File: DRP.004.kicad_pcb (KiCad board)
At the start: 4 copper layers, 55 x 27 mm, 79 parts, among them J1 Batt_conn_3p, J2 USB_C_Receptacle_PowerOnly_6P, J3 Conn_01x03_Pin, J4 Conn_01x05_Pin, J5 Conn_01x03_Pin, J6 Conn_01x03_Pin, Q1 DTC143Z, Q2 AO3400, Q3 DTC143Z, Q4 DMG1012T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

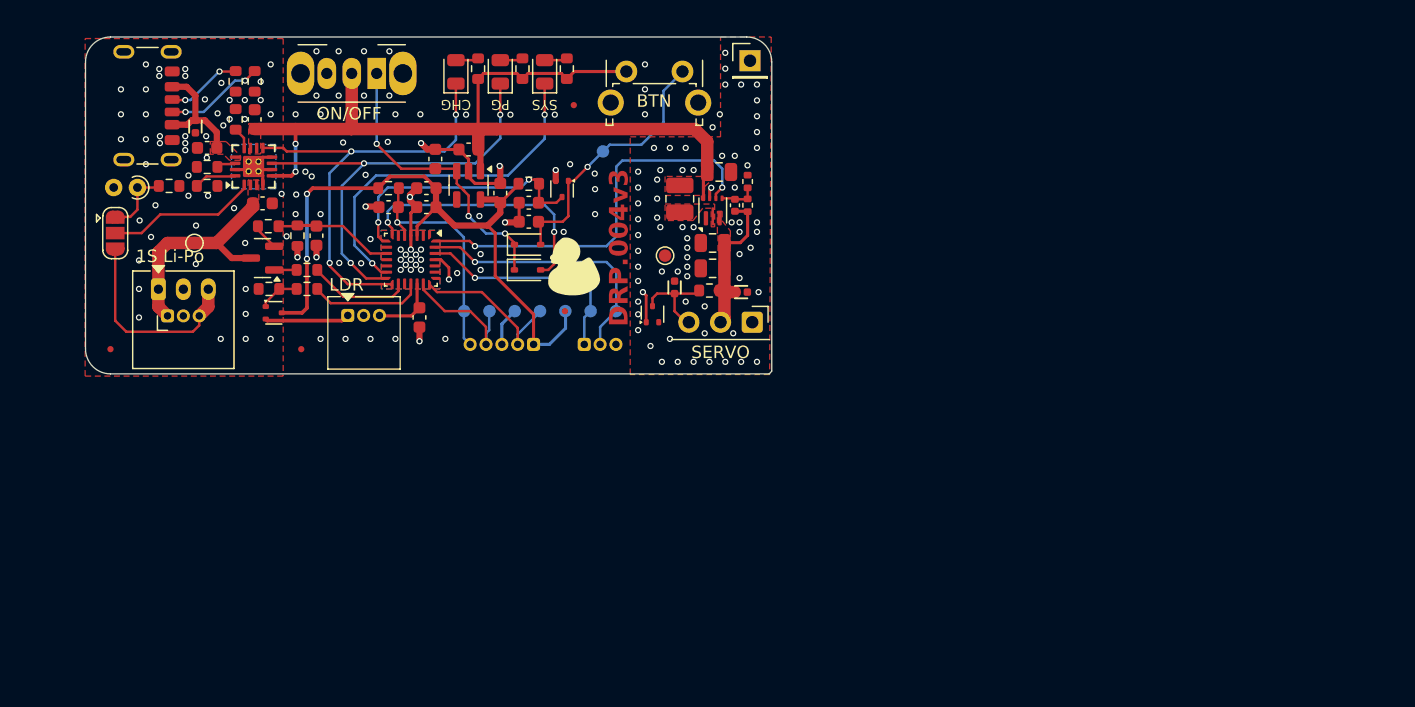
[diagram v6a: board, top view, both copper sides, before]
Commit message: Added stencil outline
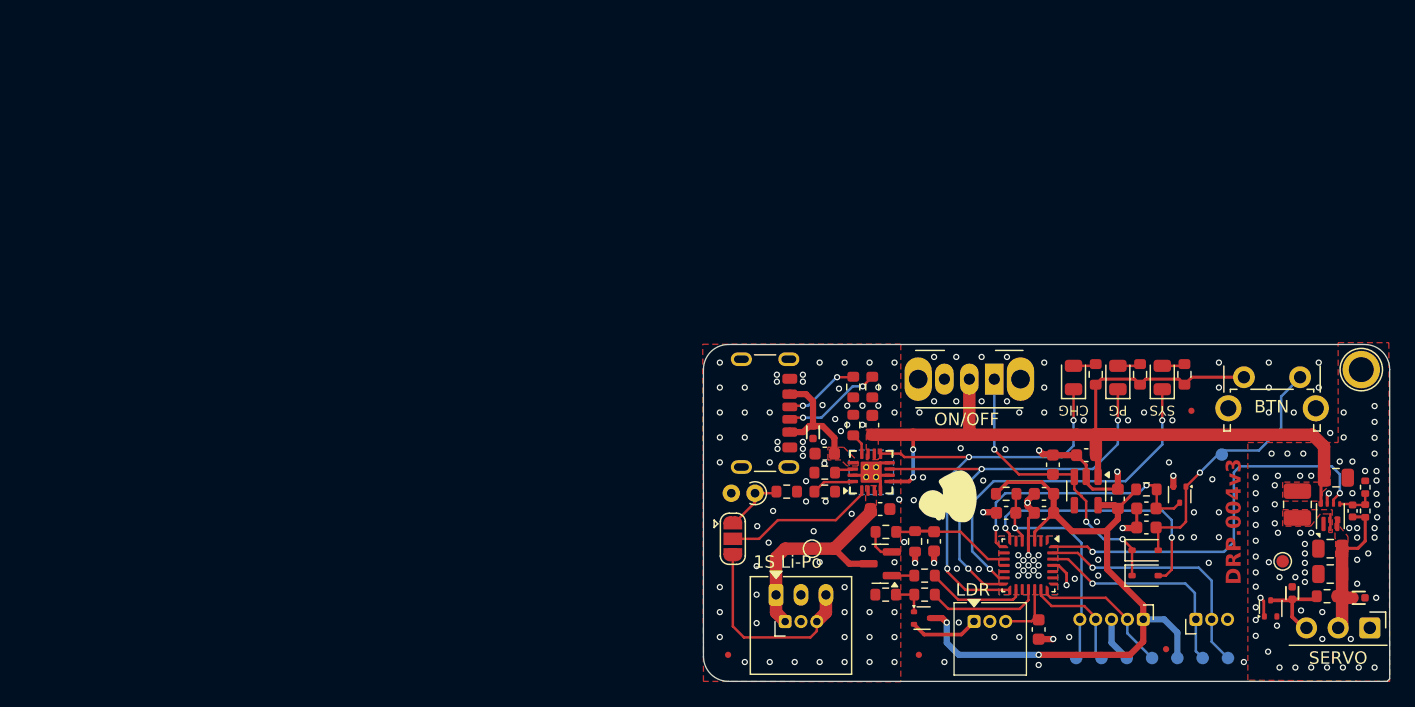
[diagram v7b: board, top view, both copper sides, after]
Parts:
- J4, J5: moved to F.Cu
- TP6: footprint Connector_PinHeader_2.54mm:PinHeader_1x01_P2.54mm_Vertical -> TestPoint:TestPoint_Plated_Hole_D2.0mm
- moved Q4 57.4 mm to (174.5, 92.9)
- moved TP1 56.4 mm to (197.0, 96.1)
- moved TP10 56.4 mm to (195.0, 96.1)
- moved TP2 56.4 mm to (199.0, 96.1)
- moved TP4 56.4 mm to (188.9, 96.1)
- moved TP5 56.4 mm to (186.9, 96.1)
- moved TP8 56.4 mm to (190.9, 96.1)
- moved TP9 56.4 mm to (193.0, 96.1)
- moved J6 55.9 mm to (178.7, 93.2)
- moved C16 55.6 mm to (183.9, 93.8)
- moved J2 55.3 mm to (160.8, 76.5)
- moved FID2 55.3 mm to (194.1, 95.4)
- moved TP11 55.2 mm to (198.5, 79.8)
- moved C1 55.2 mm to (170.5, 77.5)
- moved C10 55.2 mm to (192.5, 84.1)
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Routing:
- net +1V8: track 53.3 -> 55.6 mm
- net SWDIO: track 10.8 -> 9.03 mm
- net SWCLK: track 13.2 -> 11.5 mm
- net USART_RX: track 21.7 -> 20.4 mm
- net Net-(J6-Pin_1): track 6.69 -> 5.61 mm
- net SERVO_PWM: track 20.8 -> 19.9 mm
- net Net-(J3-Pin_3): track 6.94 -> 6.15 mm
- net Net-(JP1-A): track 5.38 -> 4.77 mm
- net NRST: track 18.5 -> 19.1 mm
- net Net-(Q2-S): track 1.85 -> 2.36 mm
- net GND: track 34.2 -> 34.7 mm, vias 184 -> 213
- net ADC_LDR: track 5.30 -> 4.80 mm

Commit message: Expanded documentation
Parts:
- added R8: 100k, Resistor_SMD:R_0603_1608Metric, F.Cu at (171.5, 92.3)
- moved FID3 3.71 mm to (170.6, 96.0)
- moved R1 2.83 mm to (171.5, 93.9)
- moved R13 1.29 mm to (174.5, 90.8)
- moved R22 1.29 mm to (174.5, 92.3)
- moved C9 1.22 mm to (175.3, 88.0)
- moved Q2 1.22 mm to (171.0, 89.8)
- moved Q4 1.22 mm to (174.3, 94.1)
- moved R17 1.22 mm to (173.8, 88.0)
- moved R16 1.21 mm to (171.5, 87.2)
- moved J1 0.22 mm to (162.6, 91.1)
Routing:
- net +BATT: track 17.5 -> 19.7 mm
- net Net-(Q2-G): track 1.69 -> 3.38 mm
- net +1V8: track 55.6 -> 54.5 mm
- net Net-(J1-TS): track 16.2 -> 16.9 mm
